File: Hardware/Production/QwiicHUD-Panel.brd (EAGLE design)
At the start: 97.3 x 124 mm, 426 parts, among them J10 WISECHIP_HUD_FPC, J15 WISECHIP_HUD_FPC, J20 WISECHIP_HUD_FPC, J25 WISECHIP_HUD_FPC, J30 WISECHIP_HUD_FPC, J35 WISECHIP_HUD_FPC, J4 WISECHIP_HUD_FPC, J40 WISECHIP_HUD_FPC, J45 WISECHIP_HUD_FPC, U1 AP3012, U2 AP3012, U3 AP3012, U4 AP3012, U5 AP3012, U6 AP3012, U7 AP3012, U8 AP3012, U9 AP3012

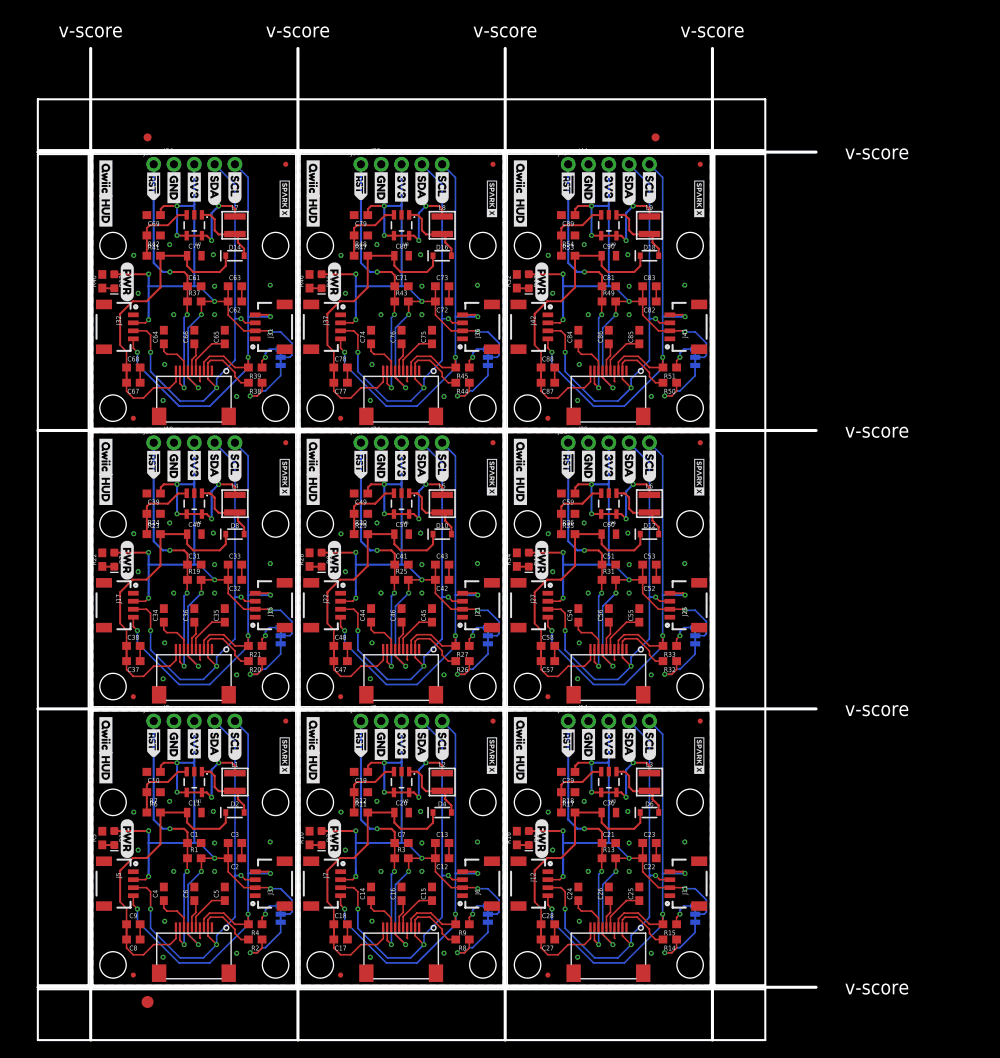
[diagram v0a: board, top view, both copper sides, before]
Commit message: Changed inductor to inventory part
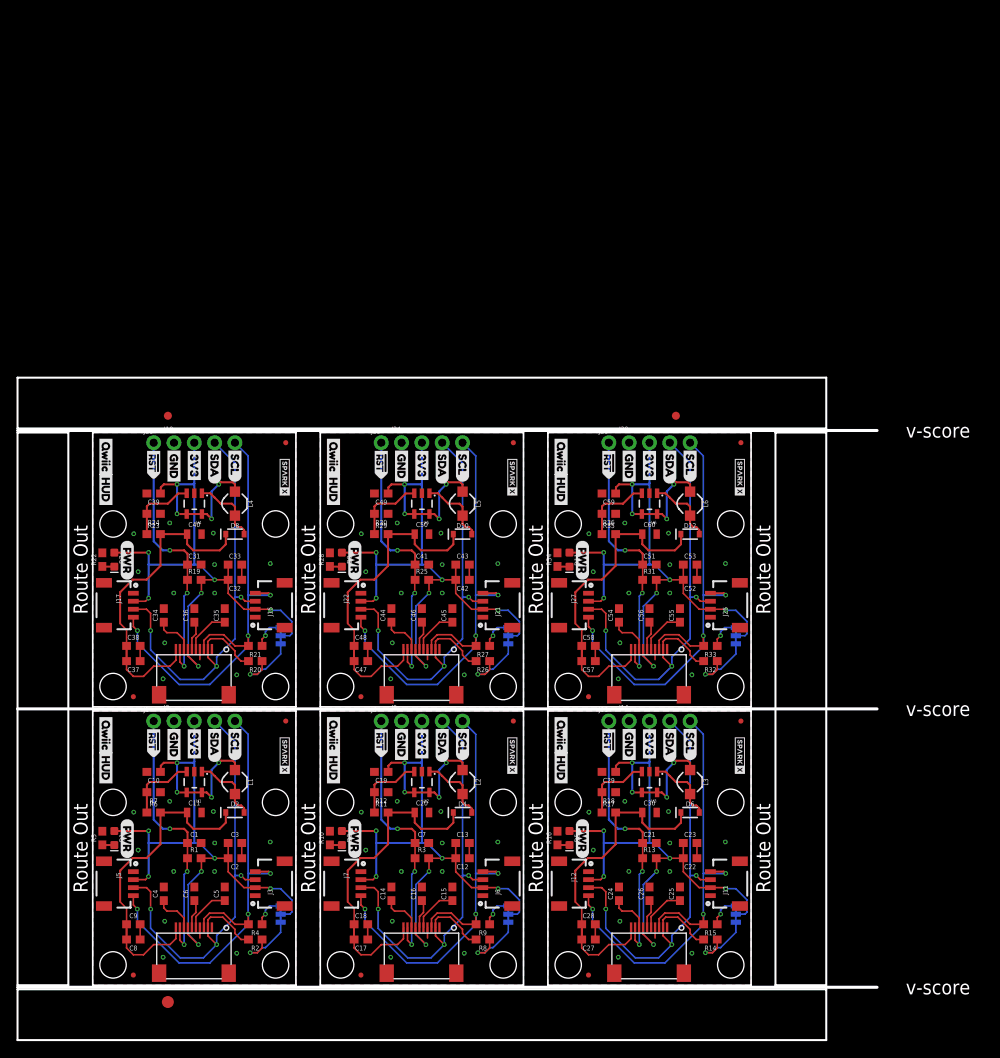
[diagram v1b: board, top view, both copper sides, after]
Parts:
- removed C61, C71, C81: 2.2uF, SparkFun-Capacitors:0603
- removed C62, C67, C72, C77, C82, C87: 4.7uF, SparkFun-Capacitors:0603
- removed C63, C68, C73, C78, C83, C88: 0.1uF, SparkFun-Capacitors:0603
- removed C64, C65, C66, C69, C74, C75, C76, C79, C84, C85, C86, C89: 1.0uF, SparkFun-Capacitors:0603
- removed C70, C80, C90: 1.0uF/25V, SparkFun-Capacitors:0805
- removed D13, D15, D17: RED, SparkFun-LED:LED-0603
- removed D14, D16, D18: 1A/23V/620mV, SparkFun-DiscreteSemi:SOD-323
- removed FD13, FD14, FD15, FD16, FD17, FD18: FIDUCIALUFIDUCIAL, SparkFun-Aesthetics:FIDUCIAL-MICRO
- removed J31, J32, J36, J37, J41, J42: (no value), SparkX:1X04_1MM_RA
- removed J33, J38, J43: (no value), SparkFun-Connectors:1X01_NO_SILK
- removed J34, J39, J44: (no value), SparkX:1X04_NO_SILK
- removed J35, J40, J45: WISECHIP_HUD_FPC, WiseChipHUD:SERIES6288
- removed JP7, JP8, JP9: (no value), SparkFun-Jumpers:SMT-JUMPER_3_2-NC_TRACE_SILK
- removed L7, L8, L9: 10uH, 1.81_Greyscale_OLED_Breakout:INDUCTOR_3X3
- removed R37, R43, R49: 10k, SparkFun-Resistors:0603
- removed R38, R39, R44, R45, R50, R51: 2.2k, SparkFun-Resistors:0603
- removed R40, R46, R52: 1k, SparkFun-Resistors:0603
- removed R41, R47, R53: 47k, SparkFun-Resistors:0603
- removed R42, R48, R54: 5.6k, SparkFun-Resistors:0603
- removed U$115, U$134, U$153: QWIIC_BOARD_OUTLINEH, SparkX:QWIIC_BOARD_MOUNT_HOLES
- removed U$116, U$117, U$135, U$136, U$154, U$155: (no value), SparkX:SPARKX-TINY
- removed U$118, U$128, U$137, U$147, U$156, U$166: (no value), Labels-0_04:#RST>
- removed U$119, U$127, U$138, U$146, U$157, U$165: (no value), Labels-0_04:GND
- removed U$120, U$126, U$139, U$145, U$158, U$164: (no value), Labels-0_04:3V3
- removed U$121, U$124, U$140, U$143, U$159, U$162: (no value), Labels-0_04:SDA
- removed U$122, U$125, U$141, U$144, U$160, U$163: (no value), Labels-0_04:SCL
- removed U$123, U$142, U$161: (no value), Labels-0_04:(PWR)
- removed U$129, U$131, U$148, U$150, U$167, U$169: (no value), buzzard_labels (1):QWIIC0
- removed U$130, U$132, U$149, U$151, U$168, U$170: (no value), buzzard_labels (1):HUD1
- removed U$133, U$152, U$171: (no value), Labels-0_04:(I_SUPER2_C)
- removed U7, U8, U9: AP3012, 1.81_Greyscale_OLED_Breakout:SOT23-5
- L1, L2, L3, L4, L5, L6: device 1.81_Greyscale_OLED_Breakout:INDUCTOR_3X3 -> SparkFun-Coils:INDUCTOR_4.7UH
- moved E$1 34.9 mm to (9.40, 71.2)
- moved E$2 34.9 mm to (72.9, 71.2)
- moved C25 5.08 mm to (73.4, 11.4)
- moved C55 5.08 mm to (73.4, 46.2)
- moved C29 5.08 mm to (64.5, 26.7)
- moved C59 5.08 mm to (64.5, 61.5)
- moved J13 5.08 mm to (64.5, 33.0)
- moved J28 5.08 mm to (64.5, 67.8)
- moved R17 5.08 mm to (64.5, 21.6)
- moved R18 5.08 mm to (64.5, 24.1)
- moved R35 5.08 mm to (64.5, 56.4)
- moved R36 5.08 mm to (64.5, 58.9)
- moved U$109 5.08 mm to (64.5, 67.6)
- moved U$42 5.08 mm to (64.5, 32.6)
- moved U$52 5.08 mm to (64.5, 32.8)
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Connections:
- removed net !RST6: C61.1, J33.1, J35.2, R37.1
- removed net !RST7: C71.1, J38.1, J40.2, R43.1
- removed net !RST8: C81.1, J43.1, J45.2, R49.1
- removed net 12V6: C67.2, C68.1, C70.1, D14.C, J35.1, R41.2
- removed net 12V7: C77.2, C78.1, C80.1, D16.C, J40.1, R47.2
- removed net 12V8: C87.2, C88.1, C90.1, D18.C, J45.1, R53.2
- removed net 3.3V6: C62.2, C63.1, C69.1, D13.A, J31.2, J32.2, J34.2, J35.4, JP7.2, L7.P$1, R37.2, U7.4, U7.5
- removed net 3.3V7: C72.2, C73.1, C79.1, D15.A, J36.2, J37.2, J39.2, J40.4, JP8.2, L8.P$1, R43.2, U8.4, U8.5
- removed net 3.3V8: C82.2, C83.1, C89.1, D17.A, J41.2, J42.2, J44.2, J45.4, JP9.2, L9.P$1, R49.2, U9.4, U9.5
- removed net GND6: C61.2, C62.1, C63.2, C64.2, C65.2, C66.2, C67.1, C68.2, C69.2, C70.2, J31.1, J32.1, J34.1, J35.10, J35.7, R40.2, R42.1, U7.2
- removed net GND7: C71.2, C72.1, C73.2, C74.2, C75.2, C76.2, C77.1, C78.2, C79.2, C80.2, J36.1, J37.1, J39.1, J40.10, J40.7, R46.2, R48.1, U8.2
- removed net GND8: C81.2, C82.1, C83.2, C84.2, C85.2, C86.2, C87.1, C88.2, C89.2, C90.2, J41.1, J42.1, J44.1, J45.10, J45.7, R52.2, R54.1, U9.2
- removed net IC19: C64.1, J35.3
- removed net IC20: C66.1, J35.5
- removed net IC21: C65.1, J35.6
- removed net IC22: C74.1, J40.3
- removed net IC23: C76.1, J40.5
- removed net IC24: C75.1, J40.6
- removed net IC25: C84.1, J45.3
- removed net IC26: C86.1, J45.5
- removed net IC27: C85.1, J45.6
- removed net N$31: JP7.3, R38.1
- removed net N$32: JP7.1, R39.1
- removed net N$33: D13.C, R40.1
- removed net N$34: D14.A, L7.P$2, U7.1
- removed net N$35: R41.1, R42.2, U7.3
- removed net N$36: JP8.3, R44.1
- removed net N$37: JP8.1, R45.1
- removed net N$38: D15.C, R46.1
- removed net N$39: D16.A, L8.P$2, U8.1
- removed net N$40: R47.1, R48.2, U8.3
- removed net N$41: JP9.3, R50.1
- removed net N$42: JP9.1, R51.1
- removed net N$43: D17.C, R52.1
- removed net N$44: D18.A, L9.P$2, U9.1
- removed net N$45: R53.1, R54.2, U9.3
- removed net SCL6: J31.4, J32.4, J34.4, J35.8, R39.2
- removed net SCL7: J36.4, J37.4, J39.4, J40.8, R45.2
- removed net SCL8: J41.4, J42.4, J44.4, J45.8, R51.2
- removed net SDA6: J31.3, J32.3, J34.3, J35.9, R38.2
- removed net SDA7: J36.3, J37.3, J39.3, J40.9, R44.2
- removed net SDA8: J41.3, J42.3, J44.3, J45.9, R50.2
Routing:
- net 3.3V7: track 93.0 -> 0.00 mm, vias 10 -> 0
- net 3.3V8: track 93.0 -> 0.00 mm, vias 10 -> 0
- net 3.3V6: track 93.0 -> 0.00 mm, vias 10 -> 0
- net SCL8: track 61.2 -> 0.00 mm, vias 3 -> 0
- net SCL7: track 61.2 -> 0.00 mm, vias 3 -> 0
- net SCL6: track 61.2 -> 0.00 mm, vias 3 -> 0
- net SDA7: track 60.3 -> 0.00 mm, vias 3 -> 0
- net SDA8: track 60.3 -> 0.00 mm, vias 3 -> 0
- net SDA6: track 60.3 -> 0.00 mm, vias 3 -> 0
- net 12V8: track 42.3 -> 0.00 mm
- net 12V7: track 42.3 -> 0.00 mm
- net 12V6: track 42.3 -> 0.00 mm
- net !RST8: track 33.8 -> 0.00 mm, vias 3 -> 0
- net !RST7: track 33.8 -> 0.00 mm, vias 3 -> 0
- net !RST6: track 33.8 -> 0.00 mm, vias 3 -> 0
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- removed copper zone on layer 1, net GND6
- removed copper zone on layer 16, net GND6
- removed copper zone on layer 1, net GND7
- removed copper zone on layer 16, net GND7
- removed copper zone on layer 1, net GND8
- removed copper zone on layer 16, net GND8
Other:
- board size 97.3 x 124 mm -> 107.4 x 82.8 mm
- board text added: "Route Out"

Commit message: Revert "Changed inductor to inventory part"
This reverts commit 6ab7a03f3320a090153a192dfaf0fd3f0c8c93f1.
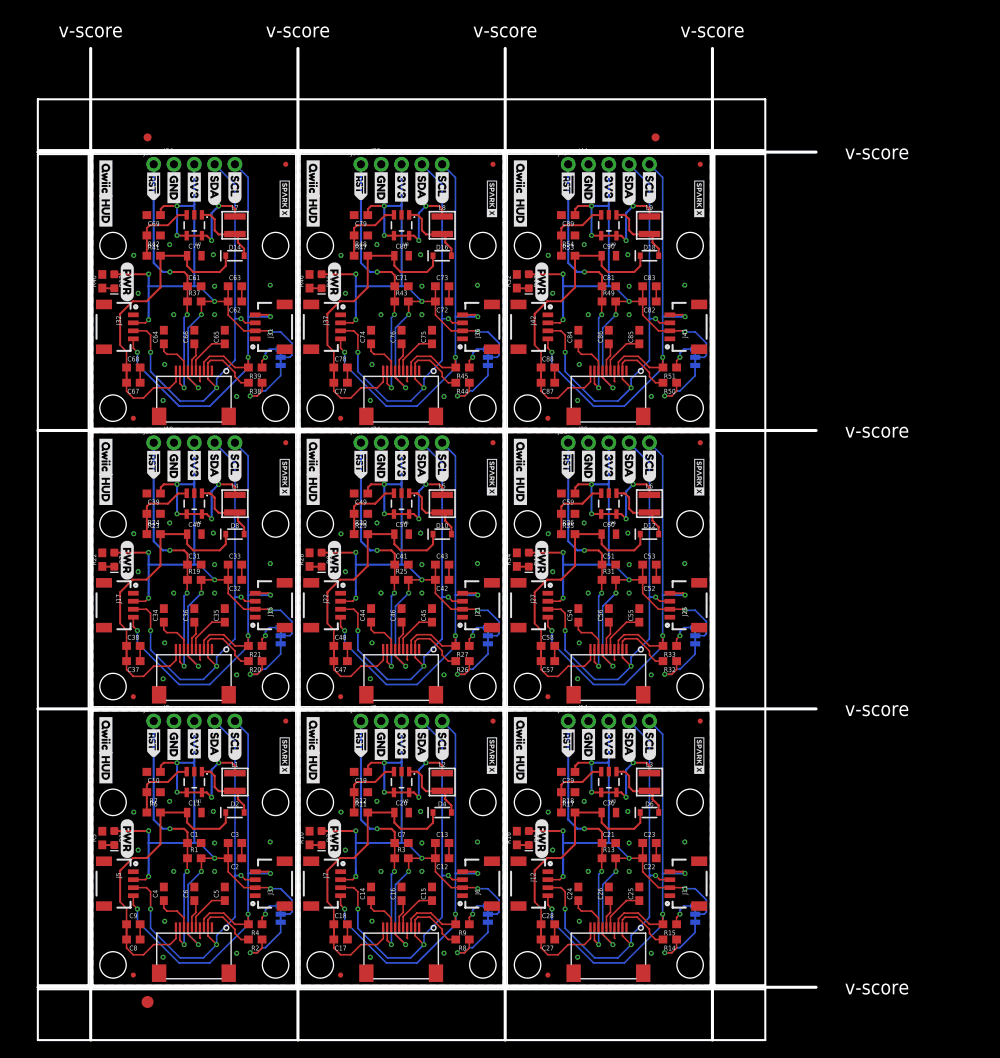
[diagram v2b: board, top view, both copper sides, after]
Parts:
- added C61, C71, C81: 2.2uF, SparkFun-Capacitors:0603
- added C62, C67, C72, C77, C82, C87: 4.7uF, SparkFun-Capacitors:0603
- added C63, C68, C73, C78, C83, C88: 0.1uF, SparkFun-Capacitors:0603
- added C64, C65, C66, C69, C74, C75, C76, C79, C84, C85, C86, C89: 1.0uF, SparkFun-Capacitors:0603
- added C70, C80, C90: 1.0uF/25V, SparkFun-Capacitors:0805
- added D13, D15, D17: RED, SparkFun-LED:LED-0603
- added D14, D16, D18: 1A/23V/620mV, SparkFun-DiscreteSemi:SOD-323
- added FD13, FD14, FD15, FD16, FD17, FD18: FIDUCIALUFIDUCIAL, SparkFun-Aesthetics:FIDUCIAL-MICRO
- added J31, J32, J36, J37, J41, J42: (no value), SparkX:1X04_1MM_RA
- added J33, J38, J43: (no value), SparkFun-Connectors:1X01_NO_SILK
- added J34, J39, J44: (no value), SparkX:1X04_NO_SILK
- added J35, J40, J45: WISECHIP_HUD_FPC, WiseChipHUD:SERIES6288
- added JP7, JP8, JP9: (no value), SparkFun-Jumpers:SMT-JUMPER_3_2-NC_TRACE_SILK
- added L7, L8, L9: 10uH, 1.81_Greyscale_OLED_Breakout:INDUCTOR_3X3
- added R37, R43, R49: 10k, SparkFun-Resistors:0603
- added R38, R39, R44, R45, R50, R51: 2.2k, SparkFun-Resistors:0603
- added R40, R46, R52: 1k, SparkFun-Resistors:0603
- added R41, R47, R53: 47k, SparkFun-Resistors:0603
- added R42, R48, R54: 5.6k, SparkFun-Resistors:0603
- added U$115, U$134, U$153: QWIIC_BOARD_OUTLINEH, SparkX:QWIIC_BOARD_MOUNT_HOLES
- added U$116, U$117, U$135, U$136, U$154, U$155: (no value), SparkX:SPARKX-TINY
- added U$118, U$128, U$137, U$147, U$156, U$166: (no value), Labels-0_04:#RST>
- added U$119, U$127, U$138, U$146, U$157, U$165: (no value), Labels-0_04:GND
- added U$120, U$126, U$139, U$145, U$158, U$164: (no value), Labels-0_04:3V3
- added U$121, U$124, U$140, U$143, U$159, U$162: (no value), Labels-0_04:SDA
- added U$122, U$125, U$141, U$144, U$160, U$163: (no value), Labels-0_04:SCL
- added U$123, U$142, U$161: (no value), Labels-0_04:(PWR)
- added U$129, U$131, U$148, U$150, U$167, U$169: (no value), buzzard_labels (1):QWIIC0
- added U$130, U$132, U$149, U$151, U$168, U$170: (no value), buzzard_labels (1):HUD1
- added U$133, U$152, U$171: (no value), Labels-0_04:(I_SUPER2_C)
- added U7, U8, U9: AP3012, 1.81_Greyscale_OLED_Breakout:SOT23-5
- L1, L2, L3, L4, L5, L6: device SparkFun-Coils:INDUCTOR_4.7UH -> 1.81_Greyscale_OLED_Breakout:INDUCTOR_3X3
- moved E$1 34.9 mm to (6.86, 106.0)
- moved E$2 34.9 mm to (70.4, 106.0)
- moved C25 5.08 mm to (68.3, 11.4)
- moved C55 5.08 mm to (68.3, 46.2)
- moved C29 5.08 mm to (59.4, 26.7)
- moved C59 5.08 mm to (59.4, 61.5)
- moved J13 5.08 mm to (59.4, 33.0)
- moved J28 5.08 mm to (59.4, 67.8)
- moved R17 5.08 mm to (59.4, 21.6)
- moved R18 5.08 mm to (59.4, 24.1)
- moved R35 5.08 mm to (59.4, 56.4)
- moved R36 5.08 mm to (59.4, 58.9)
- moved U$109 5.08 mm to (59.4, 67.6)
- moved U$42 5.08 mm to (59.4, 32.6)
- moved U$52 5.08 mm to (59.4, 32.8)
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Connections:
- new net !RST6: C61.1, J33.1, J35.2, R37.1
- new net !RST7: C71.1, J38.1, J40.2, R43.1
- new net !RST8: C81.1, J43.1, J45.2, R49.1
- new net 12V6: C67.2, C68.1, C70.1, D14.C, J35.1, R41.2
- new net 12V7: C77.2, C78.1, C80.1, D16.C, J40.1, R47.2
- new net 12V8: C87.2, C88.1, C90.1, D18.C, J45.1, R53.2
- new net 3.3V6: C62.2, C63.1, C69.1, D13.A, J31.2, J32.2, J34.2, J35.4, JP7.2, L7.P$1, R37.2, U7.4, U7.5
- new net 3.3V7: C72.2, C73.1, C79.1, D15.A, J36.2, J37.2, J39.2, J40.4, JP8.2, L8.P$1, R43.2, U8.4, U8.5
- new net 3.3V8: C82.2, C83.1, C89.1, D17.A, J41.2, J42.2, J44.2, J45.4, JP9.2, L9.P$1, R49.2, U9.4, U9.5
- new net GND6: C61.2, C62.1, C63.2, C64.2, C65.2, C66.2, C67.1, C68.2, C69.2, C70.2, J31.1, J32.1, J34.1, J35.10, J35.7, R40.2, R42.1, U7.2
- new net GND7: C71.2, C72.1, C73.2, C74.2, C75.2, C76.2, C77.1, C78.2, C79.2, C80.2, J36.1, J37.1, J39.1, J40.10, J40.7, R46.2, R48.1, U8.2
- new net GND8: C81.2, C82.1, C83.2, C84.2, C85.2, C86.2, C87.1, C88.2, C89.2, C90.2, J41.1, J42.1, J44.1, J45.10, J45.7, R52.2, R54.1, U9.2
- new net IC19: C64.1, J35.3
- new net IC20: C66.1, J35.5
- new net IC21: C65.1, J35.6
- new net IC22: C74.1, J40.3
- new net IC23: C76.1, J40.5
- new net IC24: C75.1, J40.6
- new net IC25: C84.1, J45.3
- new net IC26: C86.1, J45.5
- new net IC27: C85.1, J45.6
- new net N$31: JP7.3, R38.1
- new net N$32: JP7.1, R39.1
- new net N$33: D13.C, R40.1
- new net N$34: D14.A, L7.P$2, U7.1
- new net N$35: R41.1, R42.2, U7.3
- new net N$36: JP8.3, R44.1
- new net N$37: JP8.1, R45.1
- new net N$38: D15.C, R46.1
- new net N$39: D16.A, L8.P$2, U8.1
- new net N$40: R47.1, R48.2, U8.3
- new net N$41: JP9.3, R50.1
- new net N$42: JP9.1, R51.1
- new net N$43: D17.C, R52.1
- new net N$44: D18.A, L9.P$2, U9.1
- new net N$45: R53.1, R54.2, U9.3
- new net SCL6: J31.4, J32.4, J34.4, J35.8, R39.2
- new net SCL7: J36.4, J37.4, J39.4, J40.8, R45.2
- new net SCL8: J41.4, J42.4, J44.4, J45.8, R51.2
- new net SDA6: J31.3, J32.3, J34.3, J35.9, R38.2
- new net SDA7: J36.3, J37.3, J39.3, J40.9, R44.2
- new net SDA8: J41.3, J42.3, J44.3, J45.9, R50.2
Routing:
- net 3.3V7: track 0.00 -> 93.0 mm, vias 0 -> 10
- net 3.3V8: track 0.00 -> 93.0 mm, vias 0 -> 10
- net 3.3V6: track 0.00 -> 93.0 mm, vias 0 -> 10
- net SCL8: track 0.00 -> 61.2 mm, vias 0 -> 3
- net SCL7: track 0.00 -> 61.2 mm, vias 0 -> 3
- net SCL6: track 0.00 -> 61.2 mm, vias 0 -> 3
- net SDA7: track 0.00 -> 60.3 mm, vias 0 -> 3
- net SDA8: track 0.00 -> 60.3 mm, vias 0 -> 3
- net SDA6: track 0.00 -> 60.3 mm, vias 0 -> 3
- net 12V8: track 0.00 -> 42.3 mm
- net 12V7: track 0.00 -> 42.3 mm
- net 12V6: track 0.00 -> 42.3 mm
- net !RST8: track 0.00 -> 33.8 mm, vias 0 -> 3
- net !RST7: track 0.00 -> 33.8 mm, vias 0 -> 3
- net !RST6: track 0.00 -> 33.8 mm, vias 0 -> 3
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- added copper zone on layer 1, net GND6
- added copper zone on layer 16, net GND6
- added copper zone on layer 1, net GND7
- added copper zone on layer 16, net GND7
- added copper zone on layer 1, net GND8
- added copper zone on layer 16, net GND8
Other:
- board size 107.4 x 82.8 mm -> 97.3 x 124 mm
- board text removed: "Route Out"
